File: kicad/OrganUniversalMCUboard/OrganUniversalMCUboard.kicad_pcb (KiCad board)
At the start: 2 copper layers, 74.1 x 79.8 mm, 62 parts, among them J1 VIN (12-15V), J10 5V out, J11 GPIO, J2 EXT 5V In/out, J3 MIDI IN, J4 MIDI_THRU, J5 UART, J6 CAN, J7 I2S, J8 SPI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

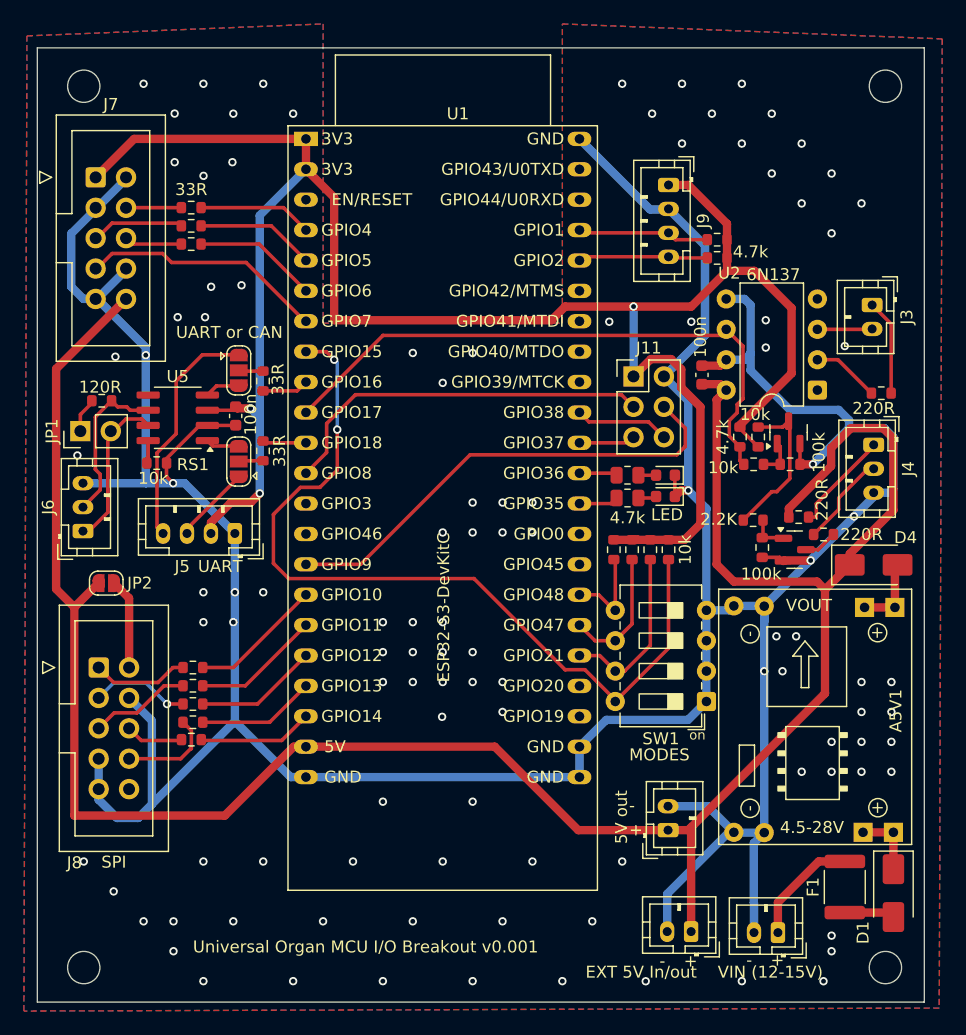
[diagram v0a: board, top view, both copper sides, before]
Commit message: Adding keyswitch breakout system, and some tools
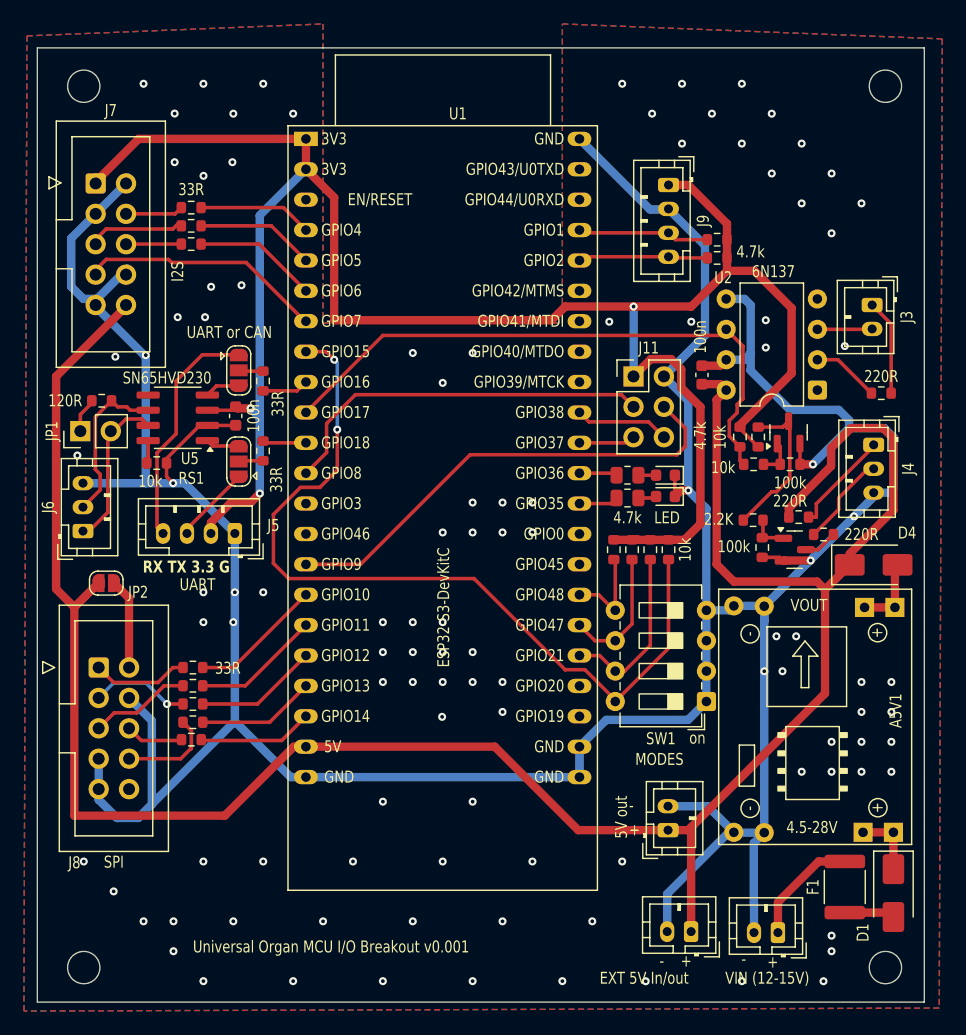
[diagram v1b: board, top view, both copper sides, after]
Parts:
- moved J7 0.51 mm to (71.0, 60.8)
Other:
- board text added: "RX TX 3.3 G"
